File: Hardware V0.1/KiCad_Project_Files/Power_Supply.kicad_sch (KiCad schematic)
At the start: 83 parts, among them J2 Conn_01x01, J3 Conn_01x01, J4 Screw_Terminal_01x02, J5 USB_C_Receptacle_USB2.0, J6 Conn_01x04, J7 Conn_01x04, Q1 FDN335N, Q2 FDN335N, SW1 UP, SW2 DW, SW3 V_I_SEL, SW4 O_EN, U1 MIC5205-5.0YM5, U2 ATmega328PB-AU, U3 TPS54531DDAR, U4 LM358, U5 INA138, U6 MCP4023-103ECH, U7 CH340E, U8 MIC5205-3.3YM5, Y1 16MHz

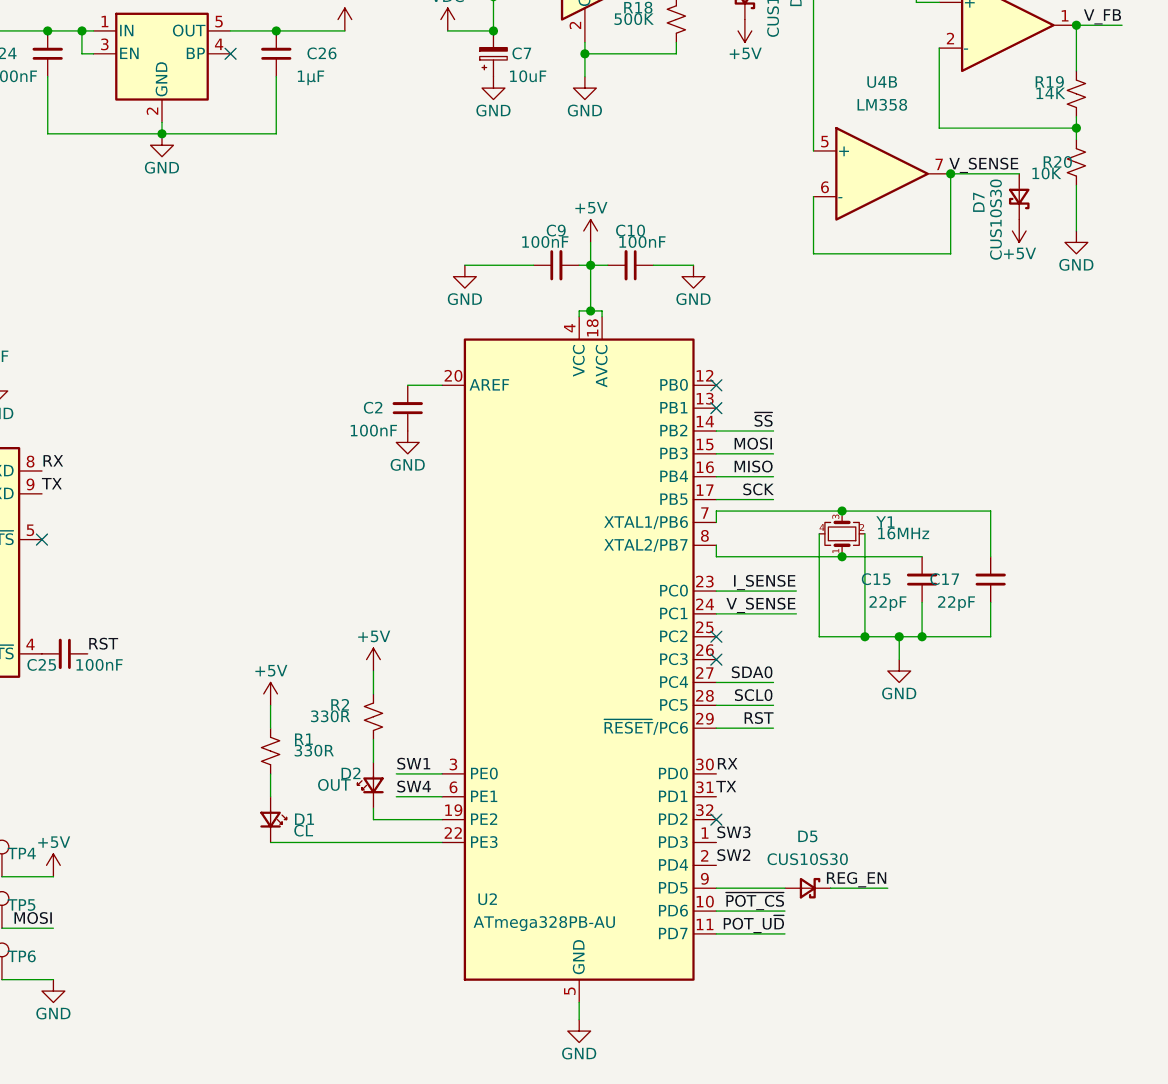
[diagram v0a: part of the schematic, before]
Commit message: changed MCU to atmega328p for easier arduino dev
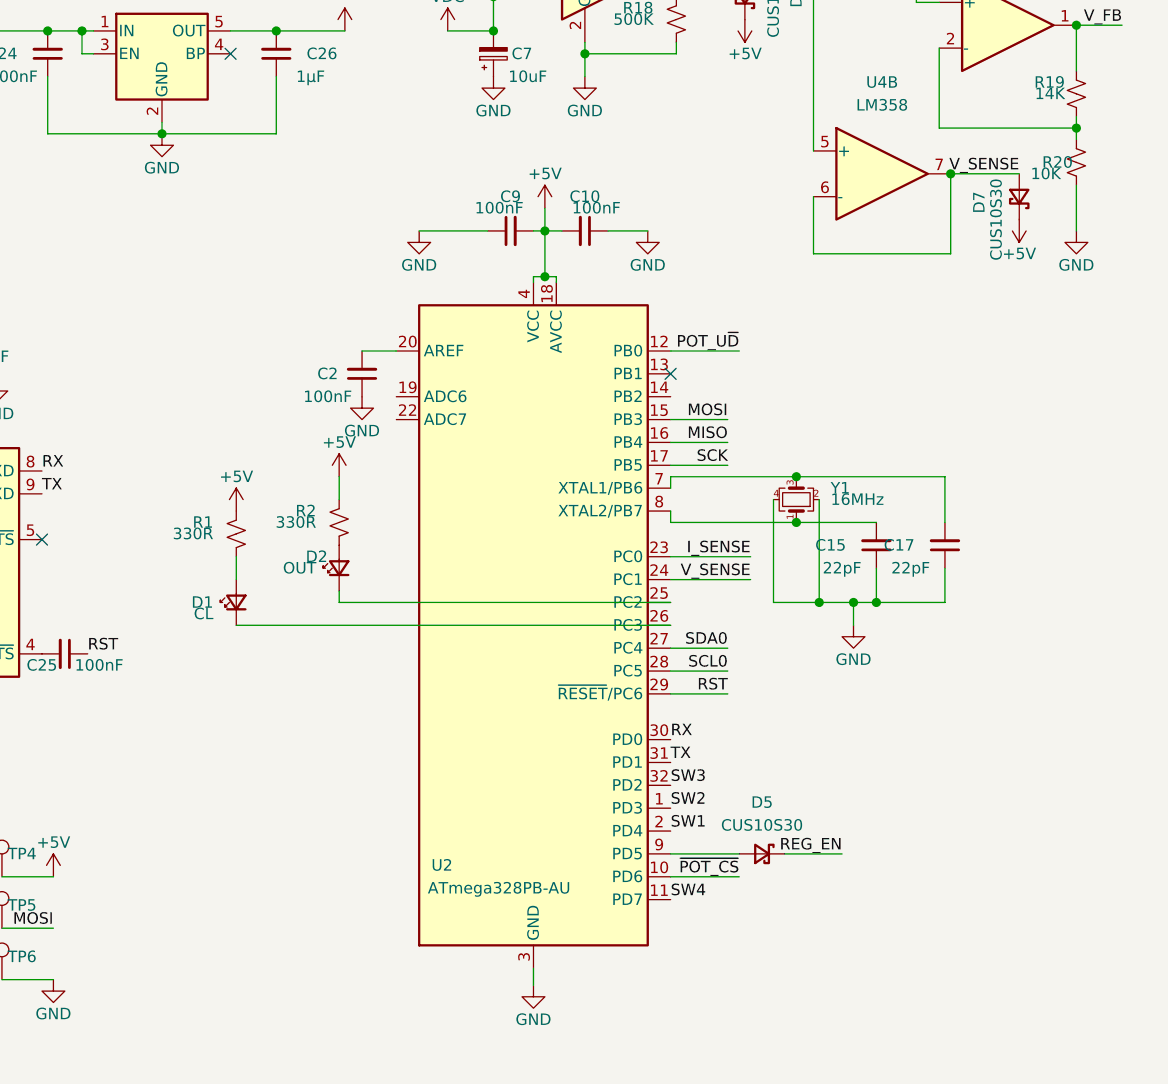
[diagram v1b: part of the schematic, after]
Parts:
- U2: symbol MCU_Microchip_ATmega:ATmega328PB-AU -> MCU_Microchip_ATmega:ATmega328P-AU
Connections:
- net +5V: now also U2.6 (VCC)
- net GND: now also U2.3 (GND)
- net POT_U~D: now also U2.12 (PB0); no longer U2.11 (PD7)
- net SW1: now also U2.2 (PD4); no longer U2.3 (PE0)
- net SW2: now also U2.1 (PD3); no longer U2.2 (PD4)
- net SW3: now also U2.32 (PD2); no longer U2.1 (PD3)
- net SW4: now also U2.11 (PD7); no longer U2.6 (PE1)
- net at D2.1 (K): now also U2.25 (PC2); no longer U2.19 (PE2)
- net at U2.22 (ADC7): no longer D1.1 (K)
- net at U2.26 (PC3): now also D1.1 (K)
- net ~SS: no longer names the net of U2.14 (PB2)
- no-connect marks 11 -> 7
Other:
- moved on the sheet: C10, C15, C17, C2, C9, D1, D2, D5, R1, R2, Y1

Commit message: subbed 0.91in with 0.96 OLED
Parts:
- added C27, C28: 100nF, Capacitor_SMD:C_0805_2012Metric, symbol Device:C_Small
- added C29, C30, C31, C33: 1µF, Capacitor_SMD:C_0805_2012Metric, symbol Device:C_Small
- added C32: 4.7µF, Capacitor_SMD:C_0805_2012Metric, symbol Device:C_Small
- added C34: 2.2µF, Capacitor_SMD:C_0805_2012Metric, symbol Device:C_Small
- added R14, R5: 2.2K, Resistor_SMD:R_0805_2012Metric, symbol Device:R_Small_US
- added R15: 390K, Resistor_SMD:R_0805_2012Metric, symbol Device:R_Small_US
- added U10: SSD1306_0.96in, Custom_Displays:SSD1306_0.96in, symbol Custom_Displays:SSD1306_0.96in
- added U9: PCA9306, Package_SO:VSSOP-8_2.3x2mm_P0.5mm, symbol Interface:PCA9306
- C21: value C_Small -> 100nF
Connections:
- net +3V3: now also C28.2, C29.2, C30.2, R14.1, R5.1, U10.11 (BS1), U10.14 (~RES), U10.15 (D/~C), U10.6 (VDDB), U10.9 (VDD), U9.7 (VREF2), U9.8 (EN)
- net +5V: now also C27.2, U9.2 (VREF1)
- net GND: now also C27.1, C28.1, C29.1, C30.1, C32.1, C34.1, R15.1, U10.1 (GND), U10.10 (BS0), U10.12 (BS2), U10.13 (~CS), U10.16 (R/~W), U10.17 (E/R~D), U10.21 (D3), U10.22 (D4), U10.23 (D5), U10.24 (D6), U10.25 (D7), U10.29 (VLSS), U10.30 (GND), U10.8 (VSS), U9.1 (GND)
- net SCL0: now also U9.3 (SCL1)
- net SDA0: now also U9.4 (SDA1)
- new net: R5.2, U10.18 (D0), U9.6 (SCL2)
- new net: R14.2, U10.19 (D1), U10.20 (D2), U9.5 (SDA2)
- new net: C33.2, U10.2 (C2P)
- new net: R15.2, U10.26 (IREF)
- new net: C32.2, U10.27 (VCOMH)
- new net: C34.2, U10.28 (VCC)
- new net: C33.1, U10.3 (C2N)
- new net: C31.1, U10.4 (C1P)
- new net: C31.2, U10.5 (C1N)
- no-connect marks 7 -> 8
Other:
- moved on the sheet: C22, C23, C25, D4, F1, J5, R10, R11, R4, R6, R8, R9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

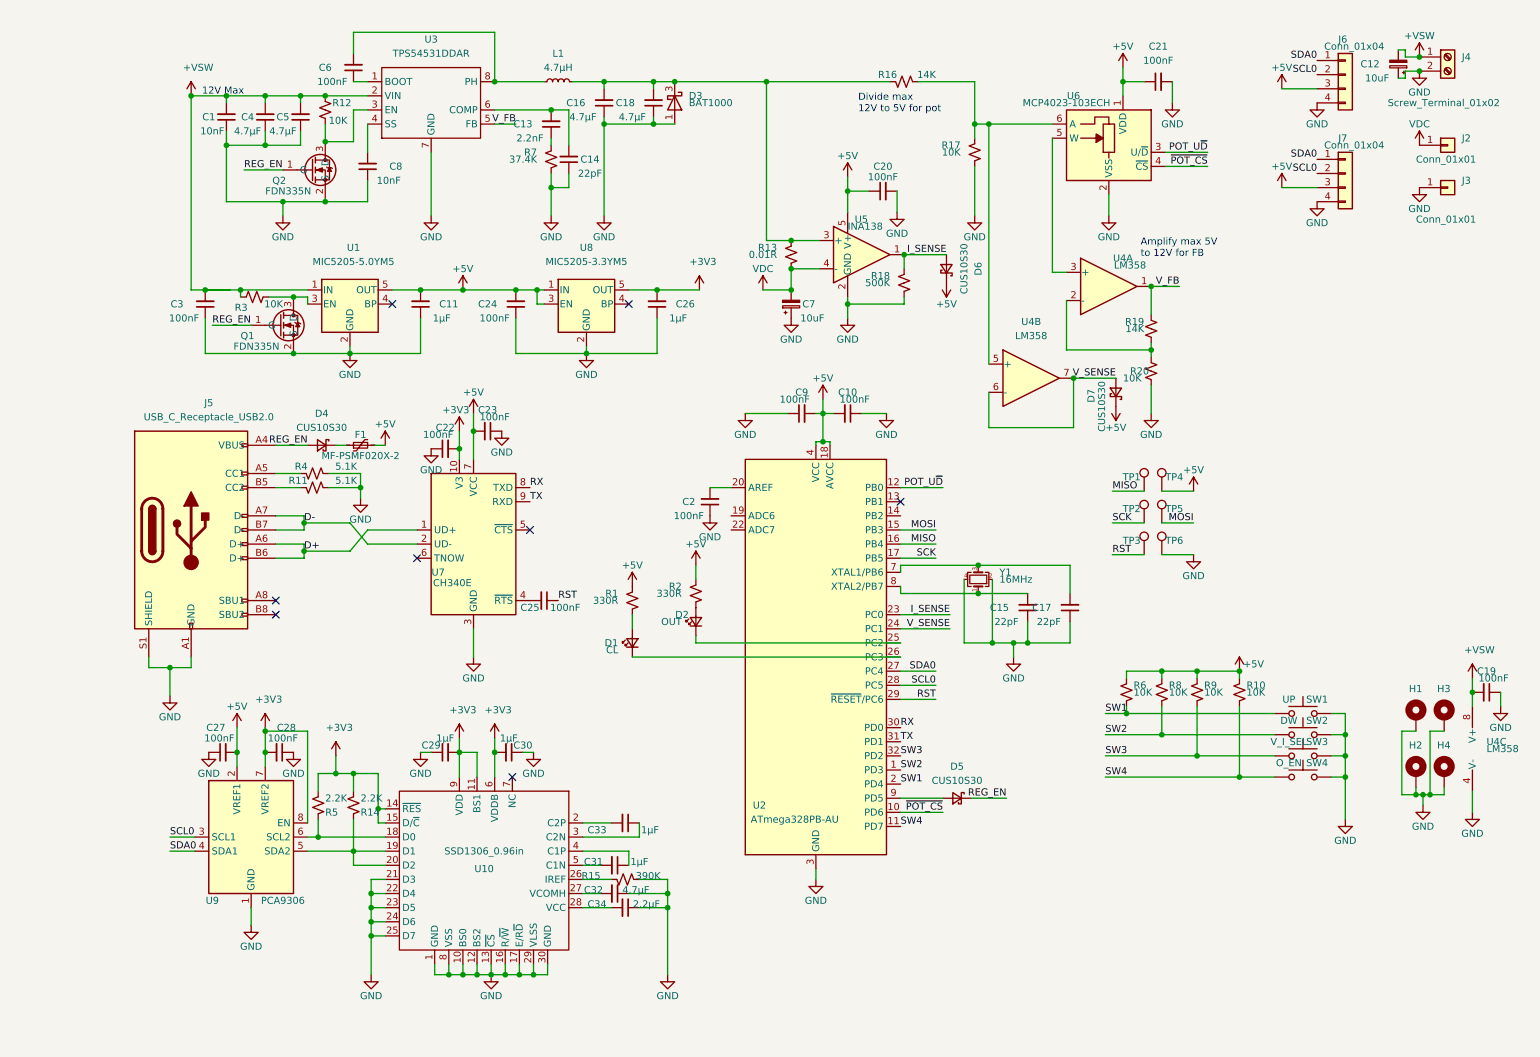
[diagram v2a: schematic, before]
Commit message: added current limiting resistors on transistors
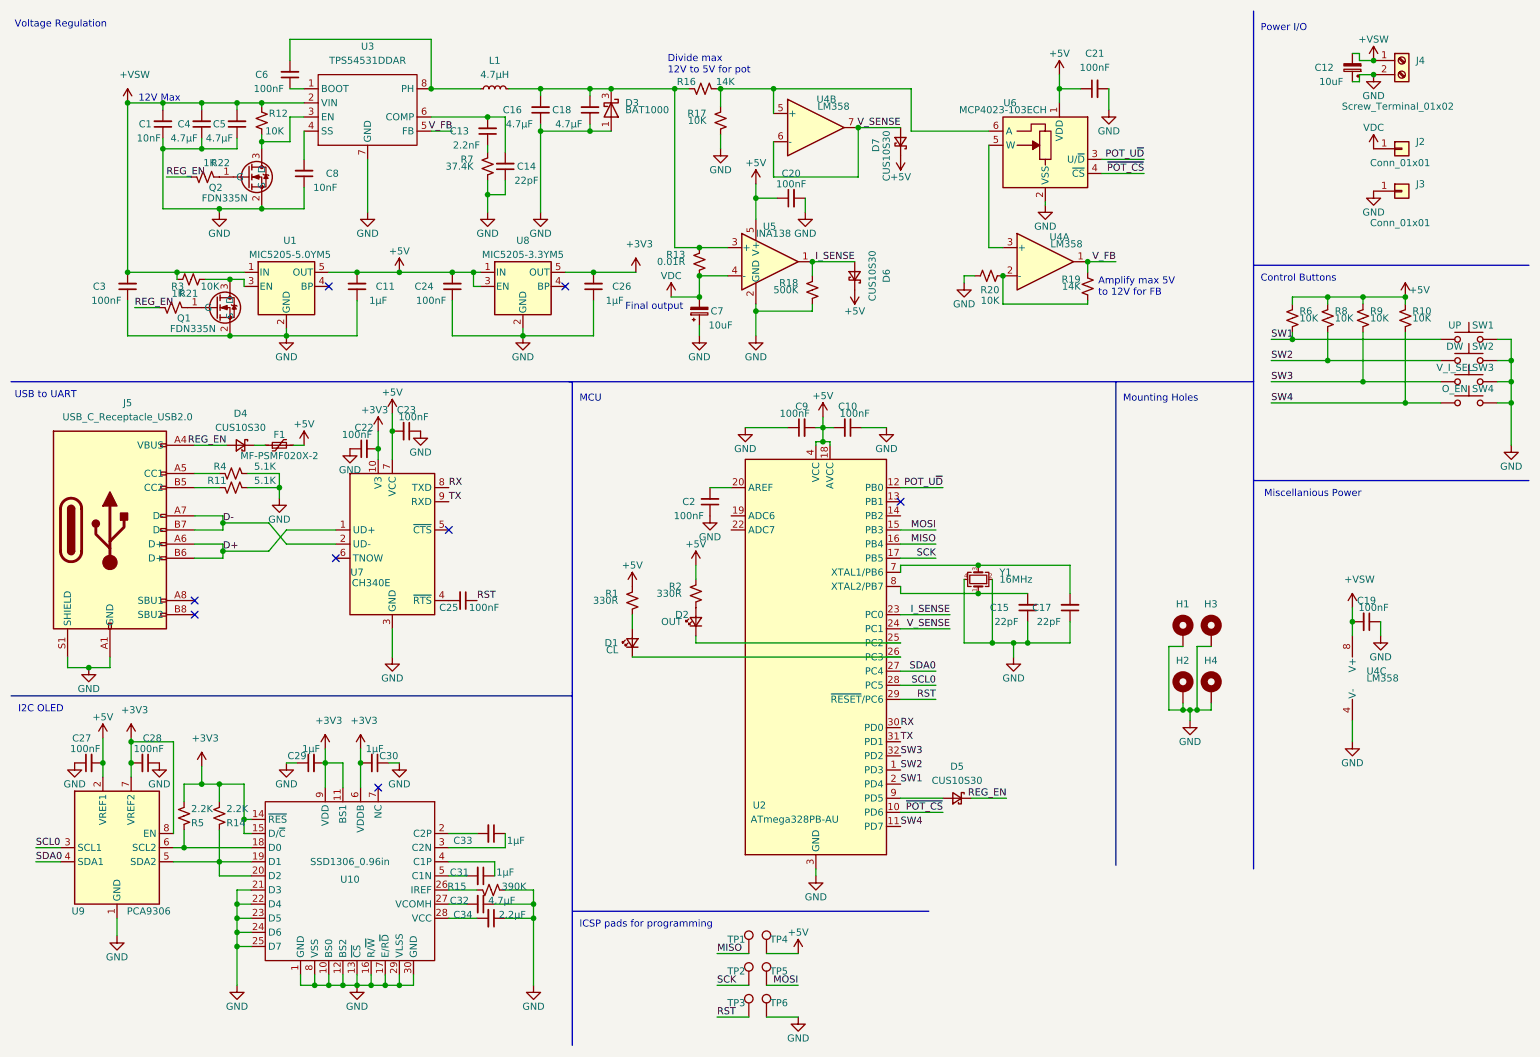
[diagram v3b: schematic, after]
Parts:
- removed J6, J7: Conn_01x04, Custom_Vertical_1x_2.54mm_Pin_Header:PinHeader_1x04_P2.54mm_Vertical, symbol Connector_Generic:Conn_01x04
- added R21, R22: 1K, Resistor_SMD:R_0805_2012Metric, symbol Device:R_Small_US
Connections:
- net GND: now also R20.2; no longer R20.1
- net REG_EN: now also R21.2, R22.2; no longer Q1.1 (G), Q2.1 (G)
- net at R19.2, U4.2 (-): now also R20.1; no longer R20.2
- new net: Q2.1 (G), R22.1
- new net: Q1.1 (G), R21.1
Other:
- note added: "Control Buttons"
- note added: "Final output"
- note added: "I2C OLED"
- note added: "ICSP pads for programming"
- note added: "MCU"
- note added: "Miscellanious Power"
- note added: "Mounting Holes"
- note added: "Power I/O"
- note added: "USB to UART"
- note added: "Voltage Regulation"
- company: (none) -> adsehgal
- title: (none) -> Benchtop Power Supply
- moved on the sheet: C1, C10, C11, C12, C13, C14, C16, C18, C19, C20, C21, C22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

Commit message: Added Vin measurement
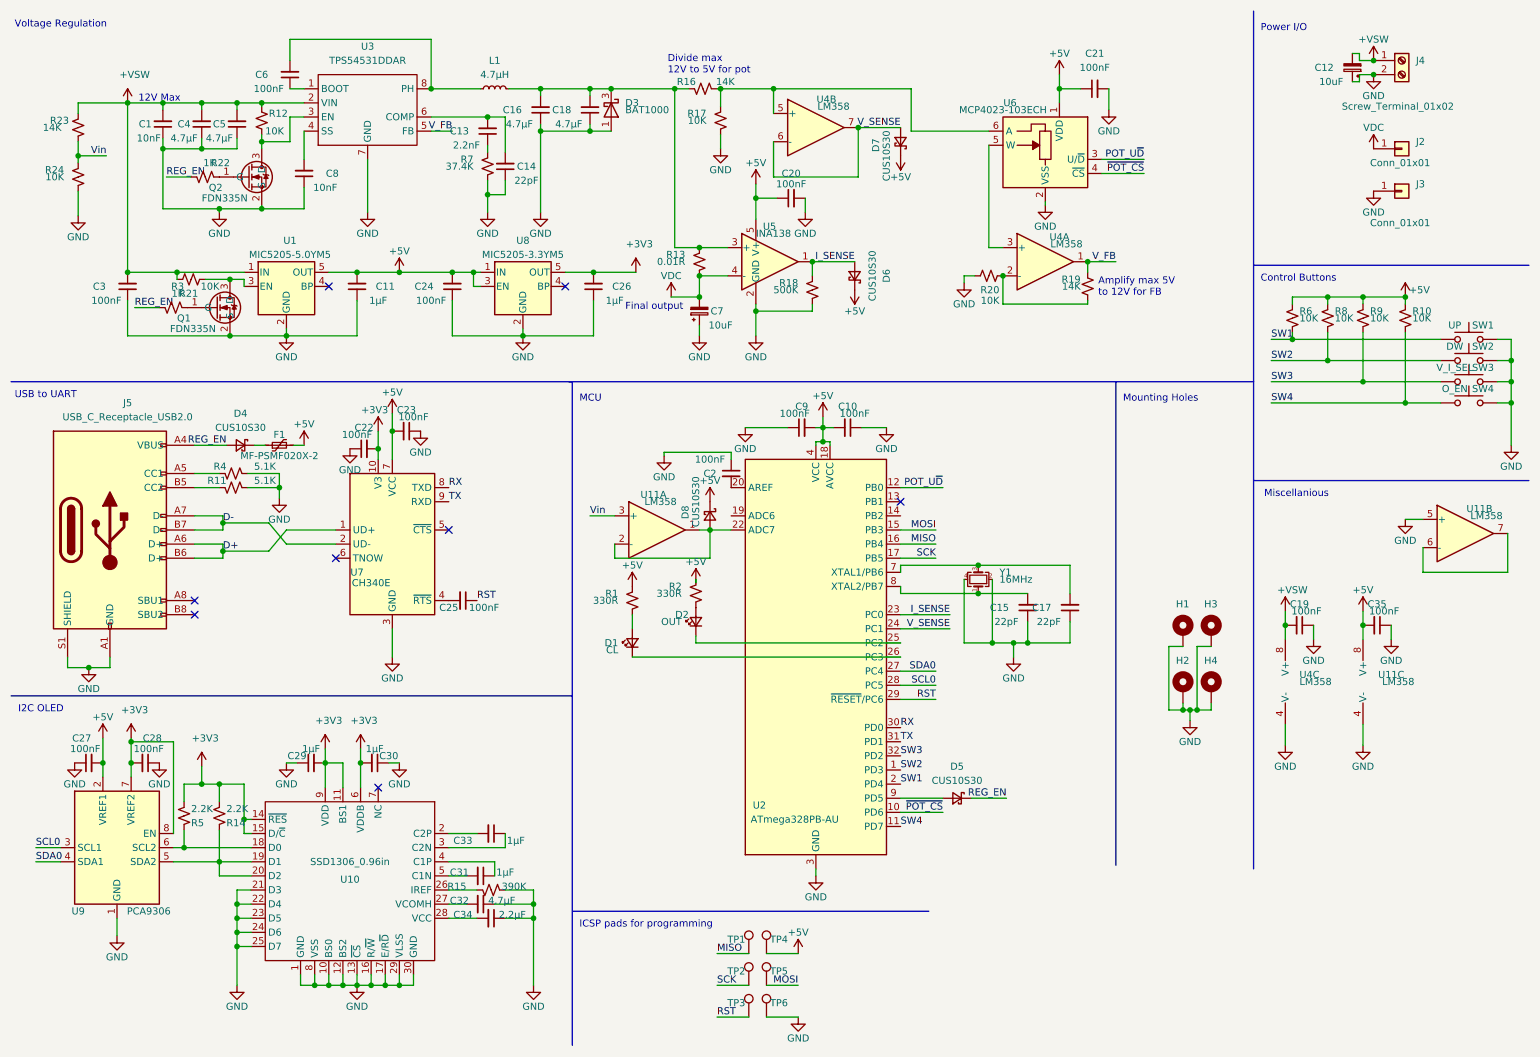
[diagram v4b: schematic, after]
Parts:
- added C35: 100nF, Capacitor_SMD:C_0805_2012Metric, symbol Device:C_Small
- added D8: CUS10S30, Diode_SMD:D_SOD-323, symbol Device:D_Schottky_Small
- added R23: 14K, Resistor_SMD:R_0805_2012Metric, symbol Device:R_Small_US
- added R24: 10K, Resistor_SMD:R_0805_2012Metric, symbol Device:R_Small_US
- added U11: LM358, Package_SO:MSOP-8_3x3mm_P0.65mm, symbol Amplifier_Operational:LM358
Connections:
- net +5V: now also C35.2, D8.1 (K), U11.8 (V+)
- net +VSW: now also R23.1
- net GND: now also C35.1, R24.1, U11.4 (V-), U11.5 (+)
- net at U2.22 (ADC7): now also D8.2 (A), U11.1, U11.2 (-)
- new net: U11.6 (-), U11.7
- new net Vin: R23.2, R24.2, U11.3 (+)
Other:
- note added: "Miscellanious"
- note removed: "Miscellanious Power"
- moved on the sheet: C19, C2, U4C
